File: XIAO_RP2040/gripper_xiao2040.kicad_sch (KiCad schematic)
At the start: 11 parts, among them J1 GoFa IO, J2 VGoFa, J3 Servo, U1 XIAO-RP2040-DIP, U2 HCPL-2631

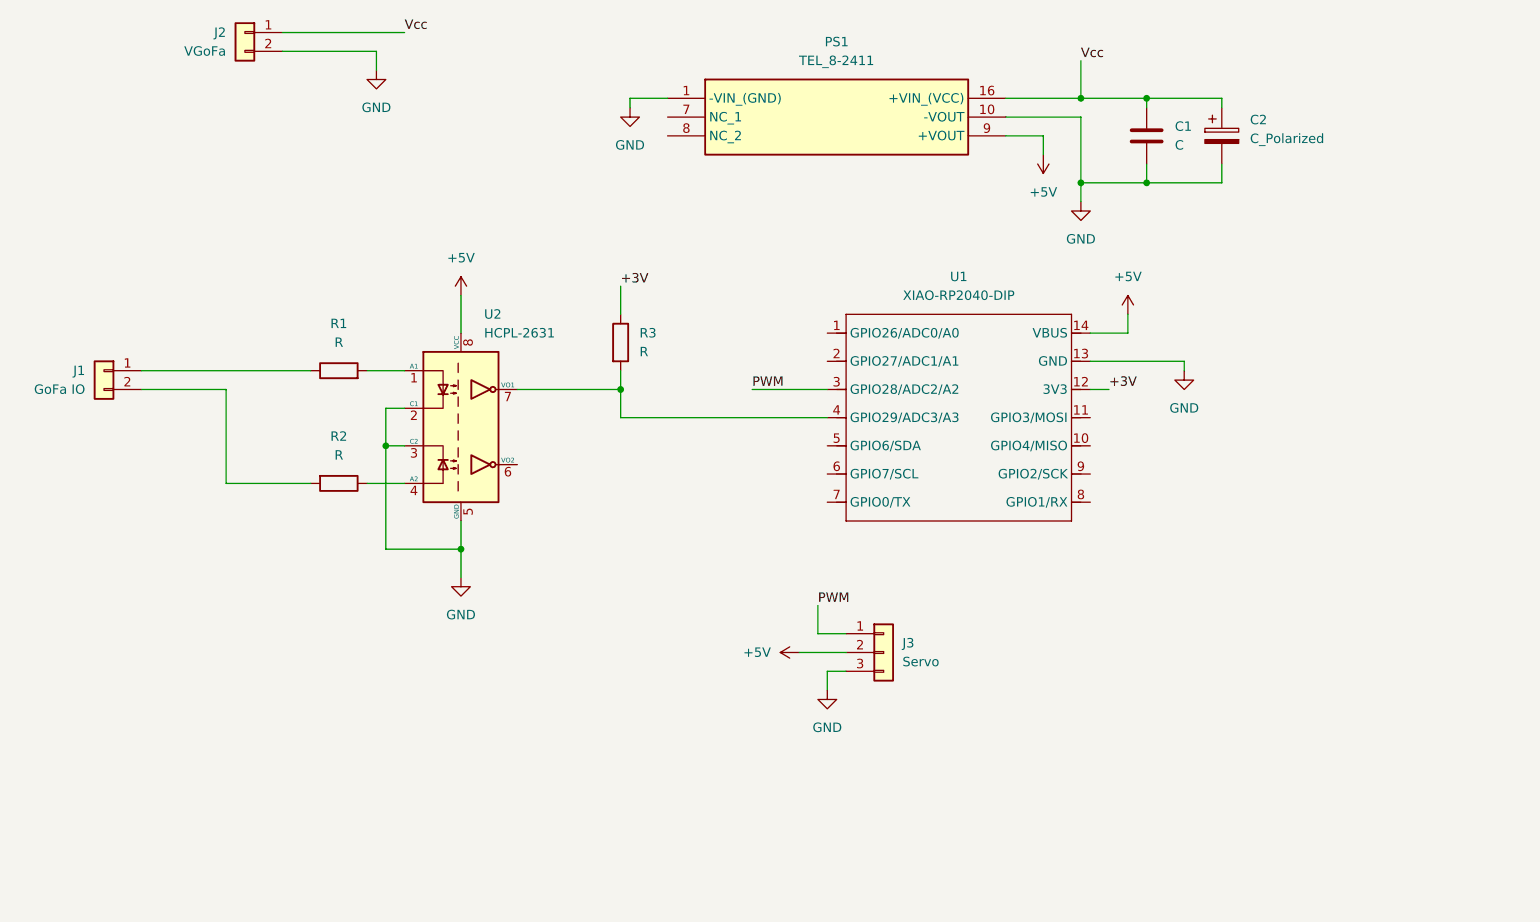
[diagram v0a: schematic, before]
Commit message: Improving PCB routing and including Arduino code
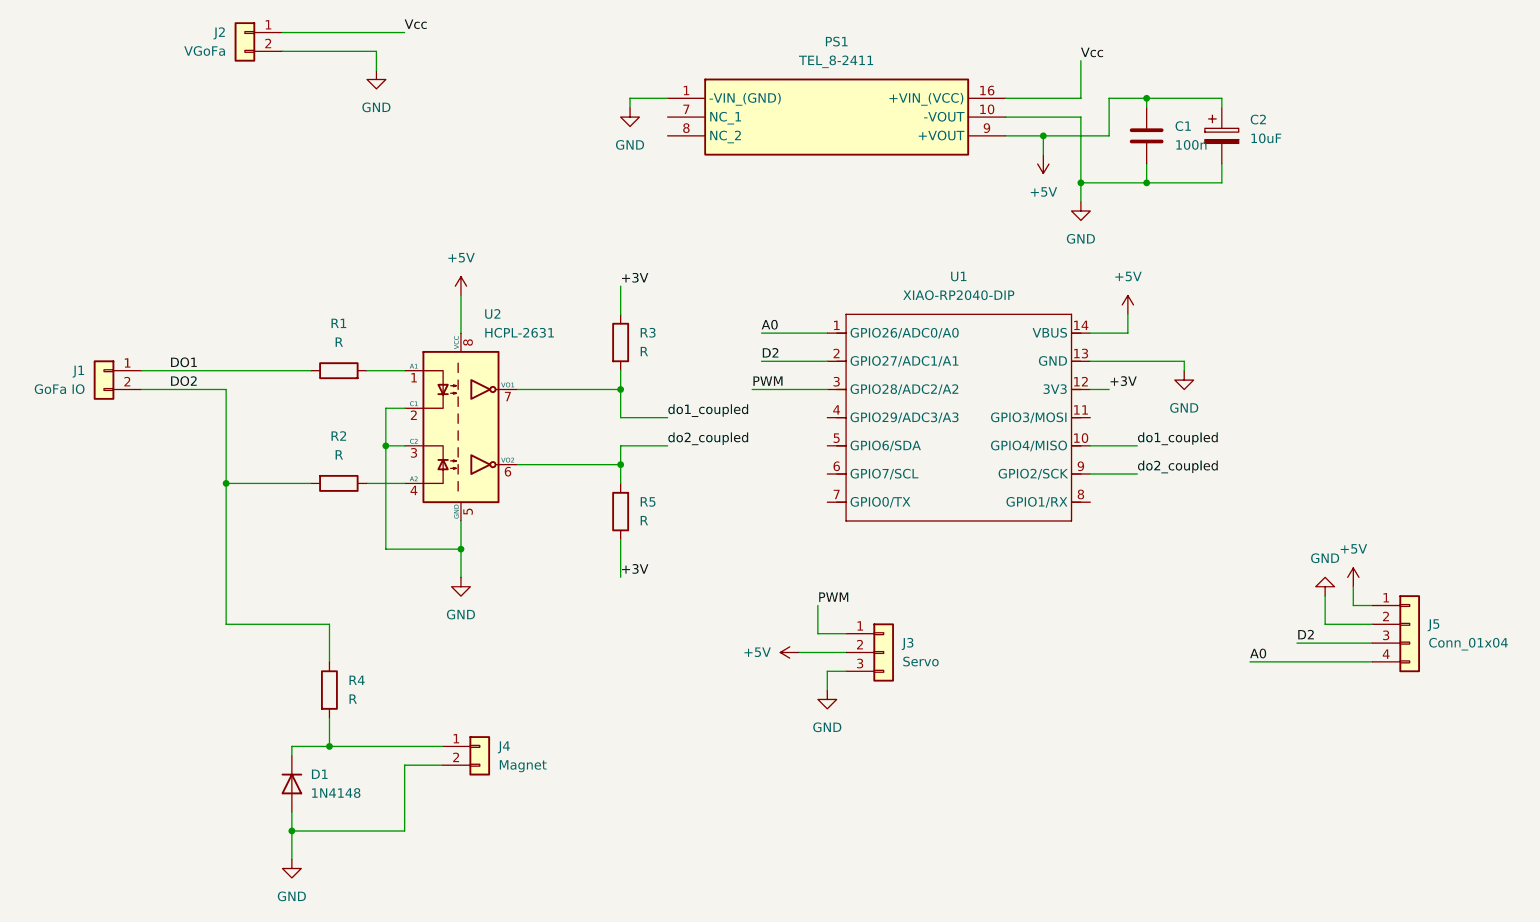
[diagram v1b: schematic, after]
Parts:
- added D1: 1N4148, Diode_THT:D_DO-35_SOD27_P7.62mm_Horizontal, symbol Diode:1N4148
- added J4: Magnet, Connector_PinHeader_2.54mm:PinHeader_1x02_P2.54mm_Vertical, symbol Connector_Generic:Conn_01x02
- added J5: Conn_01x04, Connector_PinHeader_2.54mm:PinHeader_1x04_P2.54mm_Vertical, symbol Connector_Generic:Conn_01x04
- added R4, R5: R, Resistor_SMD:R_1210_3225Metric, symbol Device:R
- C1: value C -> 100n
- C2: value C_Polarized -> 10uF
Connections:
- net +3V: now also R5.1
- net +5V: now also C1.1, C2.1, J5.1 (Pin_1)
- net GND: now also D1.2 (A), J4.2 (Pin_2), J5.2 (Pin_2)
- net Vcc: no longer C1.1, C2.1
- net DO1: now reaches J1.1 (Pin_1), R1.1
- net do1_coupled: now reaches R3.2, U2.7 (VO1)
- net do1_coupled: now also U1.10 (GPIO4/MISO); no longer U1.4 (GPIO29/ADC3/A3)
- net do2_coupled: now reaches U2.6 (VO2)
- net do2_coupled: now also U1.9 (GPIO2/SCK), R5.2
- net DO2: now reaches J1.2 (Pin_2), R2.2
- net DO2: now also R4.1
- net A0: now reaches U1.1 (GPIO26/ADC0/A0)
- net A0: now also J5.4 (Pin_4)
- net D2: now reaches U1.2 (GPIO27/ADC1/A1)
- net D2: now also J5.3 (Pin_3)
- new net: D1.1 (K), J4.1 (Pin_1), R4.2
